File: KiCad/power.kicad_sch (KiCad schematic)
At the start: 6 parts, among them K1 SRD-05VDC-SL-C, Q5 AO3400A

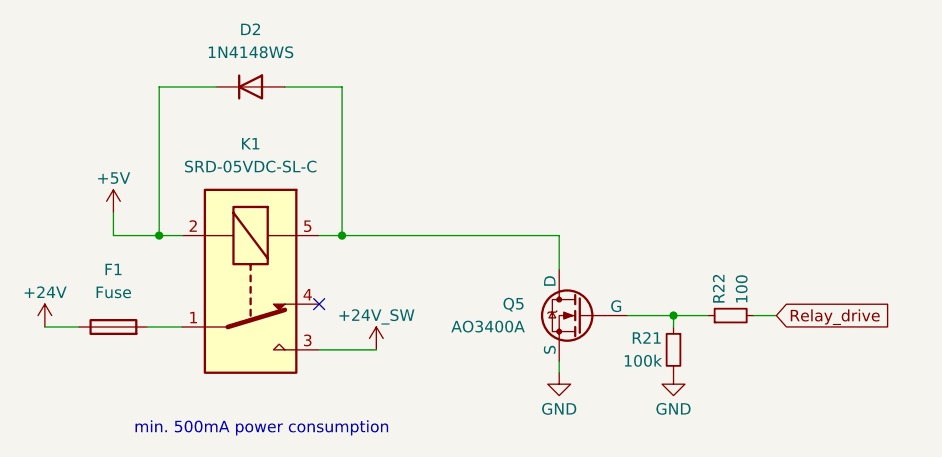
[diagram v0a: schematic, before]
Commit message: add ideal diode
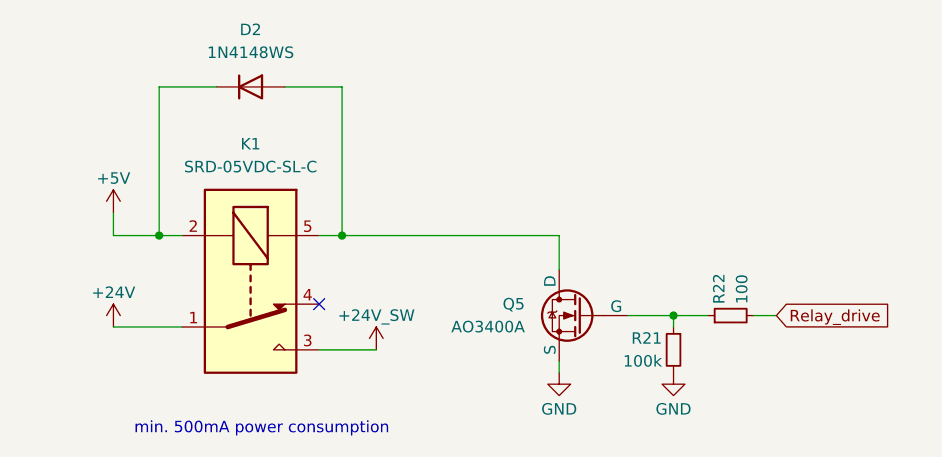
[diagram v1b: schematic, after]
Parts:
- removed F1: Fuse, Fuse:Fuseholder_Blade_Mini_Keystone_3568, symbol Device:Fuse
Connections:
- net +24V: now also K1.1
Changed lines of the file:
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@@
 	(wire
 		(pts
-			(xy 45.72 52.07) (xy 49.53 52.07)
-		)
-		(stroke
-			(width 0)
-			(type default)
-		)
-	)
-	(wire
-		(pts
-			(xy 34.29 52.07) (xy 38.1 52.07)
+			(xy 41.91 52.07) (xy 49.53 52.07)
 		)
 		(stroke
@@
 	(symbol
 		(lib_id "power:+3.3V")
-		(at 34.29 52.07 0)
+		(at 41.91 52.07 0)
 		(unit 1)
 		(body_style 1)
@@
 		(dnp no)
 		(property "Reference" "#PWR047"
-			(at 34.29 55.88 0)
+			(at 41.91 55.88 0)
 			(hide yes)
 			(show_name no)
@@
 		)
 		(property "Value" "+24V"
-			(at 34.29 48.26 0)
+			(at 41.91 48.26 0)
 			(show_name no)
 			(do_not_autoplace no)
@@
 		)
 		(property "Footprint" ""
-			(at 34.29 52.07 0)
+			(at 41.91 52.07 0)
 			(hide yes)
 			(show_name no)
@@
 		)
 		(property "Datasheet" ""
-			(at 34.29 52.07 0)
+			(at 41.91 52.07 0)
 			(hide yes)
 			(show_name no)
@@
 		)
 		(property "Description" "Power symbol creates a global label with name \"+3.3V\""
-			(at 34.29 52.07 0)
+			(at 41.91 52.07 0)
 			(hide yes)
 			(show_name no)
@@
 					(unit 1)
 				)
-			)
-		)
-	)
-	(symbol
-		(lib_id "Device:Fuse")
-		(at 41.91 52.07 90)
-		(unit 1)
-		(body_style 1)
-		(exclude_from_sim no)
-		(in_bom yes)
-		(on_board yes)
-		(in_pos_files yes)
-		(dnp no)
-		(fields_autoplaced yes)
-		(property "Reference" "F1"
-			(at 41.91 45.72 90)
-			(show_name no)
-			(do_not_autoplace no)
-			(effects
-				(font
-					(size 1.27 1.27)
-				)
-			)
-		)
-		(property "Value" "Fuse"
-			(at 41.91 48.26 90)
-			(show_name no)
-			(do_not_autoplace no)
-			(effects
-				(font
-					(size 1.27 1.27)
-				)
-			)
-		)
-		(property "Footprint" "Fuse:Fuseholder_Blade_Mini_Keystone_3568"
-			(at 41.91 53.848 90)
-			(hide yes)
-			(show_name no)
-			(do_not_autoplace no)
-			(effects
-				(font
-					(size 1.27 1.27)
-				)
-			)
-		)
-		(property "Datasheet" ""
-			(at 41.91 52.07 0)
-			(hide yes)
-			(show_name no)
-			(do_not_autoplace no)
-			(effects
-				(font
-					(size 1.27 1.27)
-				)
-			)
-		)
-		(property "Description" "Fuse"
-			(at 41.91 52.07 0)
-			(hide yes)
-			(show_name no)
-			(do_not_autoplace no)
-			(effects
-				(font
-					(size 1.27 1.27)
-				)
-			)
-		)
-		(property "LCSC" "C19727305"
-			(at 41.91 52.07 0)
-			(hide yes)
-			(show_name no)
-			(do_not_autoplace no)
-			(effects
-				(font
-					(size 1.27 1.27)
-				)
-			)
-		)
-		(pin "2"
-		)
-		(pin "1"
-		)
-		(instances
-			(project "LEDController"
-				(path "/4e4f96d2-86d5-4a03-8de9-74109a01887a/591fc044-0465-4e00-94a2-1406fe940325"
-					(reference "F1")
-					(unit 1)
-				)

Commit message: add esd protection, pullup on EN, Replicate layout
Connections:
- net +24V renamed VCC_IN
- net +24V_SW renamed VCC_SW
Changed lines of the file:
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@@
 			)
 		)
-		(property "Value" "+24V_SW"
+		(property "Value" "VCC_SW"
 			(at 71.12 50.8 0)
 			(show_name no)
@@
 			)
 		)
-		(property "Value" "+24V"
+		(property "Value" "VCC_IN"
 			(at 41.91 48.26 0)
 			(show_name no)
